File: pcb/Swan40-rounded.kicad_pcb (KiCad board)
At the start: 2 copper layers, 268 x 89.1 mm, 104 parts, among them SW1 SW_PUSH, SW10 SW_PUSH, SW11 SW_PUSH, SW12 SW_PUSH, SW13 SW_PUSH, SW14 SW_PUSH, SW15 SW_PUSH, SW16 SW_PUSH, SW17 SW_DPDT_x2, SW18 SW_PUSH, SW19 SW_PUSH, SW2 SW_PUSH, SW20 SW_PUSH, SW21 SW_PUSH, SW22 SW_PUSH, SW23 SW_PUSH, SW24 SW_PUSH, SW25 SW_PUSH, SW26 SW_PUSH, SW27 SW_PUSH, SW28 SW_PUSH, SW29 SW_PUSH, SW3 SW_PUSH, SW30 SW_PUSH, SW31 SW_PUSH, SW32 SW_PUSH, SW33 SW_PUSH, SW34 SW_DPDT_x2, SW35 SW_PUSH, SW36 SW_PUSH, SW37 SW_PUSH, SW38 SW_PUSH, SW39 SW_PUSH, SW4 SW_PUSH, SW40 SW_PUSH, SW41 SW_PUSH, SW42 SW_PUSH, SW5 SW_PUSH, SW6 SW_PUSH, SW7 SW_PUSH, SW8 SW_PUSH, SW9 SW_PUSH, U1 xiao_nrf52840, U2 xiao_nrf52840

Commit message: Refactored folders, added plates
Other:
- board size 268 x 89.1 mm -> 268 x 88.8 mm
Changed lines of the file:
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@@
   (gr_line (start 128.25 63.75) (end 140.75 63.75)
     (stroke (width 0.1) (type default)) (layer "Edge.Cuts"))
-  (gr_line (start 168.5 42.5) (end 170.75 42.5)
+  (gr_line (start 168.5 42.5) (end 172.25 42.5)
     (stroke (width 0.1) (type default)) (layer "Edge.Cuts"))
   (gr_line (start 146 63.75) (end 146 43.75)
     (stroke (width 0.1) (type default)) (layer "Edge.Cuts"))
-  (gr_arc (start 170.75 42.5) (mid 231.850316 36.364041) (end 281.5 72.5)
+  (gr_arc (start 172.25 42.5) (mid 232.570591 36.758555) (end 281.5 72.5)
     (stroke (width 0.1) (type default)) (layer "Edge.Cuts"))
   (gr_line (start 149 63.75) (end 149 43.75)
@@
   (gr_arc (start 82 112.5) (mid 47.710213 111.181348) (end 13.5 108.5)
     (stroke (width 0.1) (type default)) (layer "Edge.Cuts"))
-  (gr_line (start 126.5 42.5) (end 124.25 42.5)
+  (gr_line (start 126.5 42.5) (end 122.75 42.5)
     (stroke (width 0.1) (type default)) (layer "Edge.Cuts"))
   (gr_line (start 13.5 72.5) (end 13.5 108.5)
@@
   (gr_arc (start 167.25 63.25) (mid 167.103553 63.603553) (end 166.75 63.75)
     (stroke (width 0.1) (type default)) (layer "Edge.Cuts"))
-  (gr_arc (start 13.5 72.5) (mid 63.149681 36.364033) (end 124.25 42.5)
+  (gr_arc (start 13.5 72.5) (mid 62.429407 36.758548) (end 122.75 42.5)
     (stroke (width 0.1) (type default)) (layer "Edge.Cuts"))
   (gr_arc (start 149 43.75) (mid 149.366117 42.866117) (end 150.25 42.5)

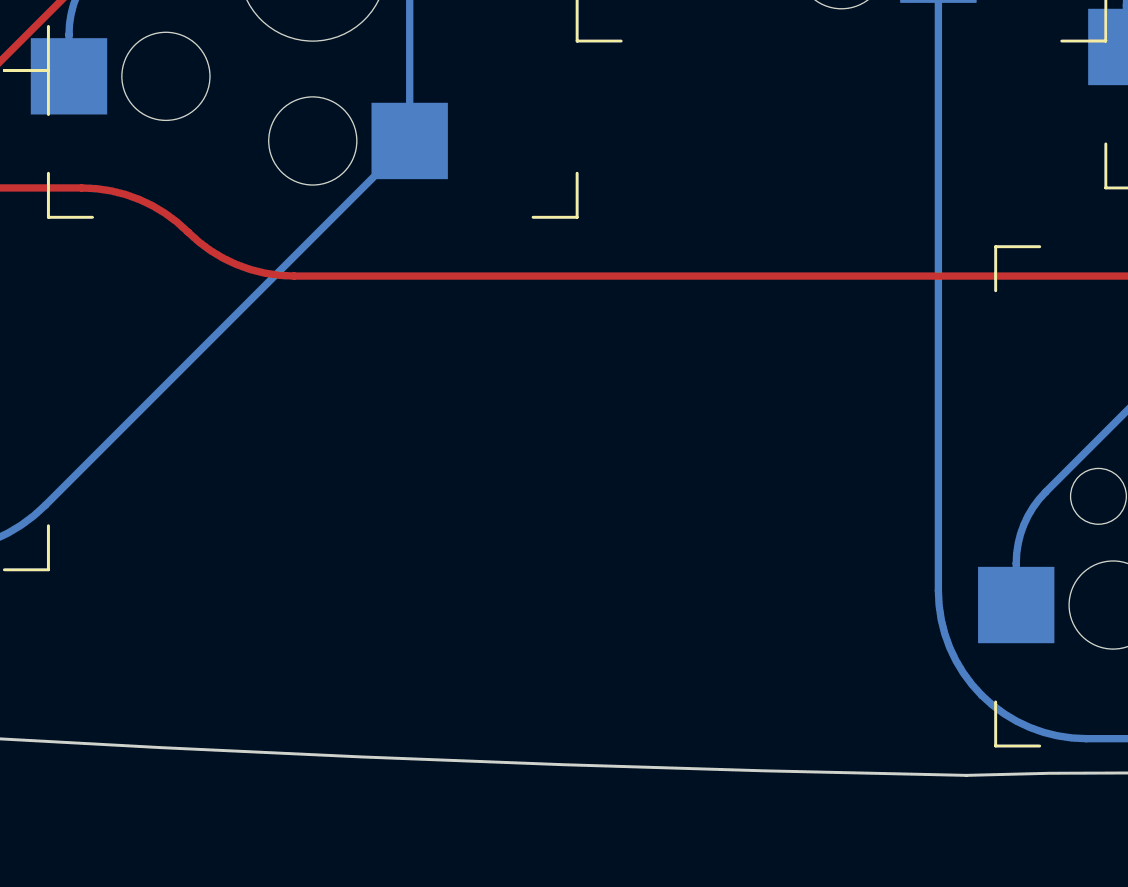
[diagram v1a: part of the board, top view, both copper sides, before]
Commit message: Added reversable plate
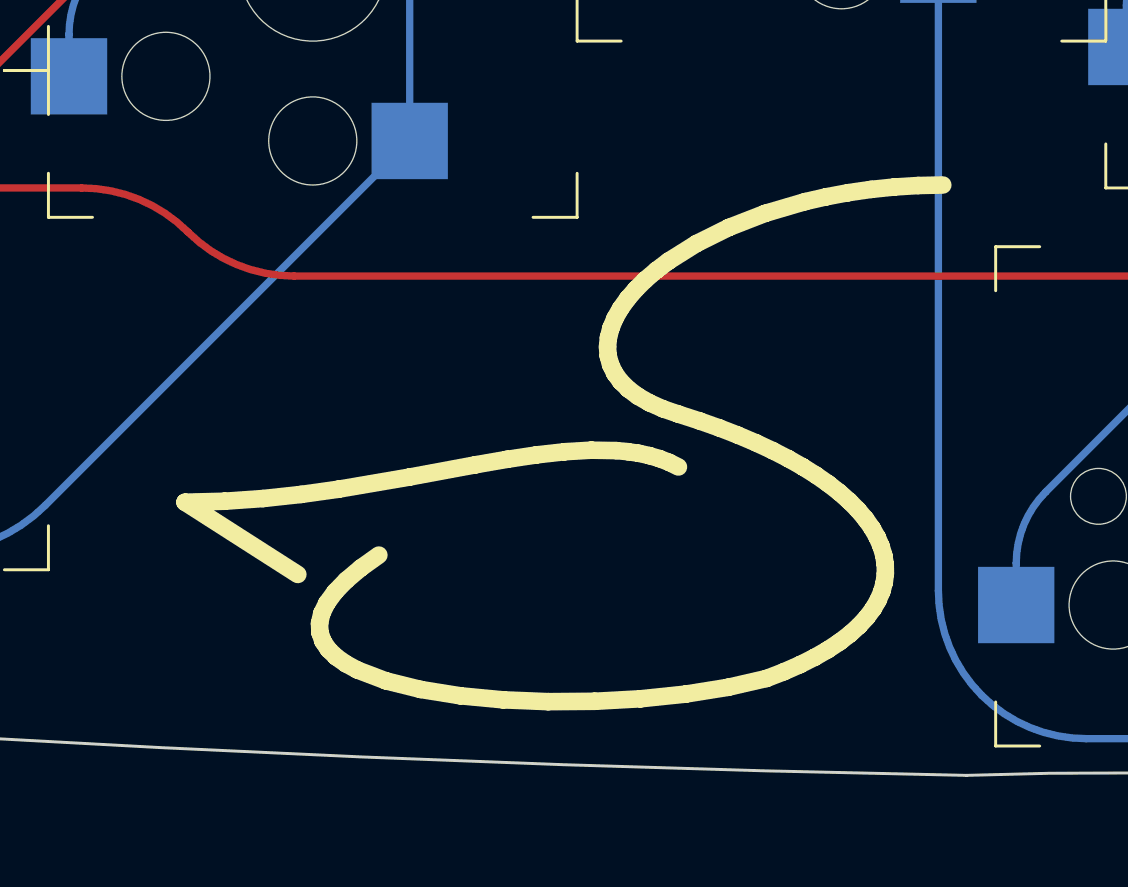
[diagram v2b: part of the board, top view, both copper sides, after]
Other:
- board text added: "Designed by shzhe02"
